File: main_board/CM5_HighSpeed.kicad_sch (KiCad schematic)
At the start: 16 parts, among them J1 USB3_A, J10 Conn_01x22_Female, J11 501568-0607-TR325, J12 SM04B-XSRS-ETBLFSN, J13 SM10B-XSRS-ETB, J22 690-019-298-412, U12 RT9742SNGV, U6 AP22653W6

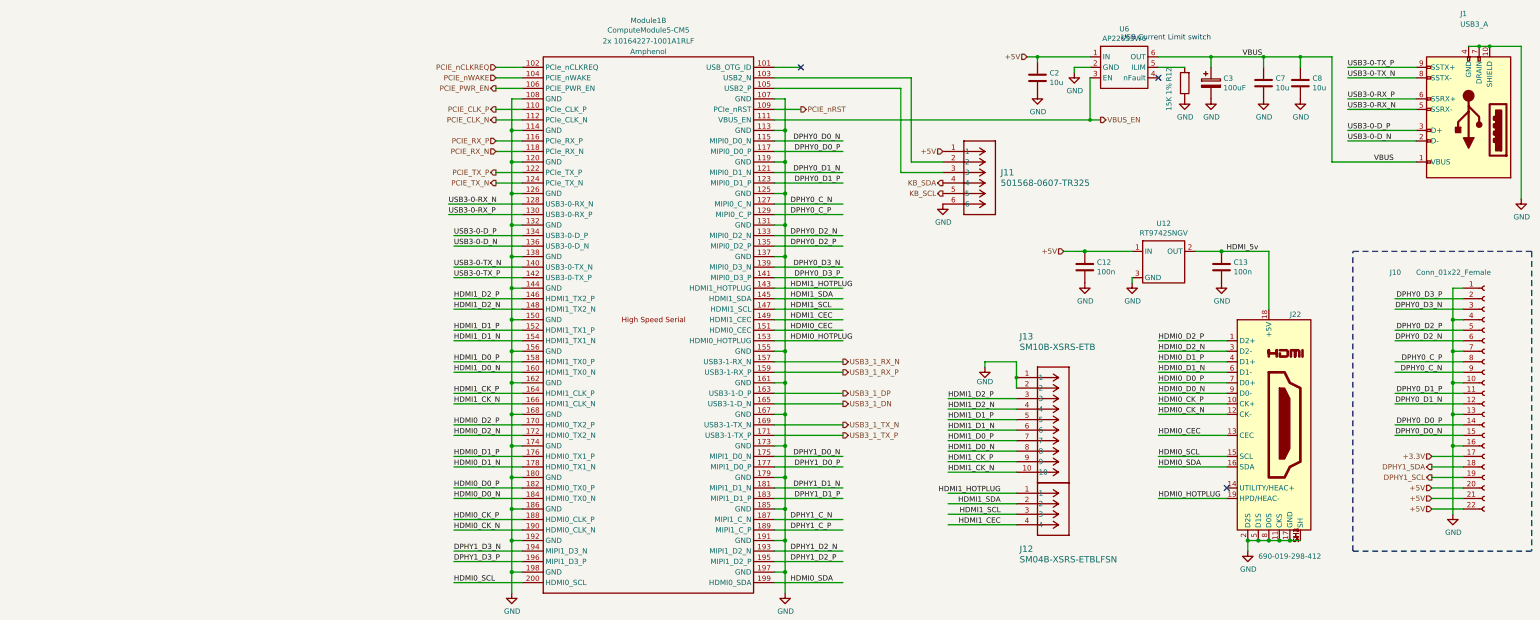
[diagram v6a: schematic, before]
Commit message: Add mounting points to symbols
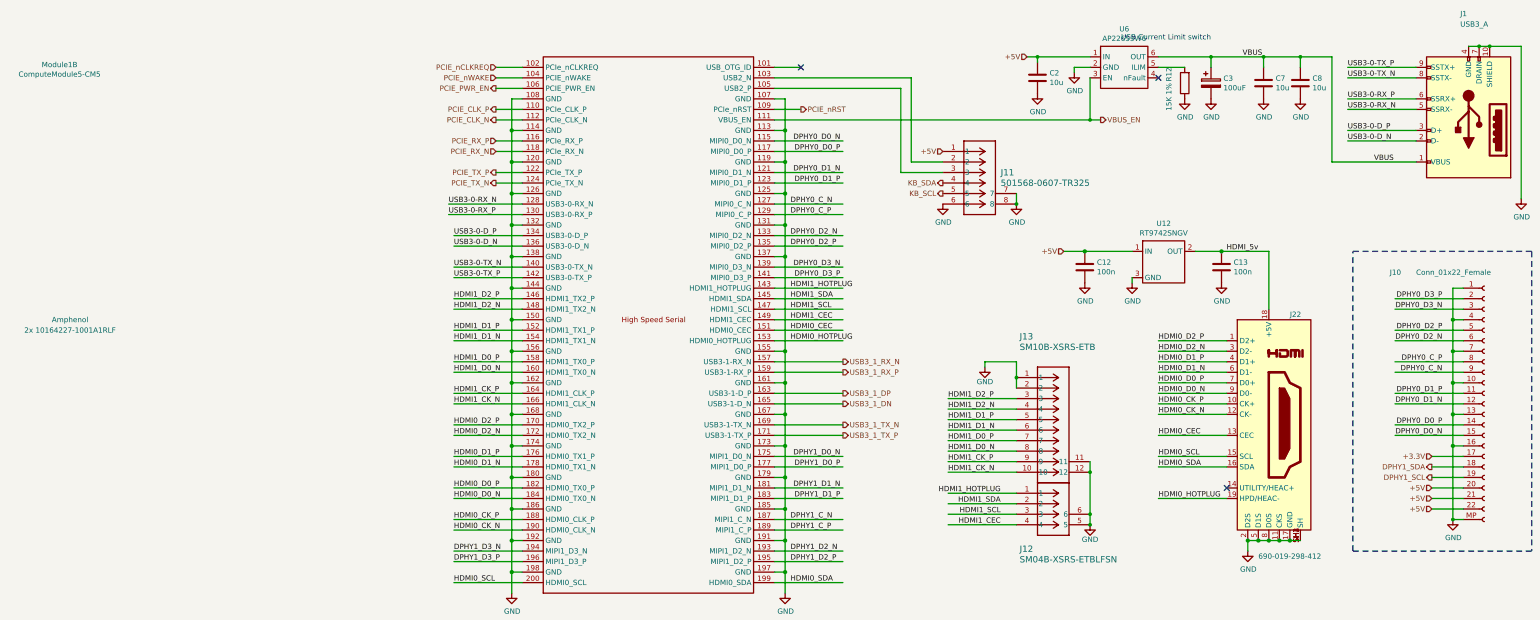
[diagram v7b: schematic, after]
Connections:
- net GND: now also J10.MP, J11.7, J11.8, J12.5, J12.6, J13.11, J13.12
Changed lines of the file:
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@@
 	)
 	(junction
+		(at 262.89 134.62)
+		(diameter 0)
+		(color 0 0 0 0)
+	)
+	(junction
 		(at 35.56 147.32)
 		(diameter 1.016)
@@
 	)
 	(junction
+		(at 157.48 58.42)
+		(diameter 0)
+		(color 0 0 0 0)
+	)
+	(junction
+		(at 175.26 135.89)
+		(diameter 0)
+		(color 0 0 0 0)
+	)
+	(junction
 		(at 35.56 78.74)
 		(diameter 1.016)
@@
 	)
 	(junction
+		(at 175.26 123.19)
+		(diameter 0)
+		(color 0 0 0 0)
+	)
+	(junction
 		(at 35.56 48.26)
 		(diameter 1.016)
@@
 	)
 	(junction
+		(at 175.26 133.35)
+		(diameter 0)
+		(color 0 0 0 0)
+	)
+	(junction
 		(at 35.56 124.46)
 		(diameter 1.016)
@@
 	(wire
 		(pts
+			(xy 157.48 55.88) (xy 157.48 58.42)
+		)
+		(stroke
+			(width 0)
+			(type default)
+		)
+	)
+	(wire
+		(pts
 			(xy 35.56 139.7) (xy 35.56 147.32)
 		)
@@
 	(wire
 		(pts
+			(xy 175.26 133.35) (xy 175.26 135.89)
+		)
+		(stroke
+			(width 0)
+			(type default)
+		)
+	)
+	(wire
+		(pts
 			(xy 171.45 25.4) (xy 171.45 26.67)
 		)
@@
 	(wire
 		(pts
+			(xy 262.89 134.62) (xy 265.43 134.62)
+		)
+		(stroke
+			(width 0)
+			(type default)
+		)
+	)
+	(wire
+		(pts
 			(xy 99.06 121.92) (xy 115.57 121.92)
 		)
@@
 	(wire
 		(pts
+			(xy 175.26 120.65) (xy 175.26 123.19)
+		)
+		(stroke
+			(width 0)
+			(type default)
+		)
+	)
+	(wire
+		(pts
 			(xy 20.32 60.96) (xy 38.1 60.96)
 		)
@@
 	(wire
 		(pts
+			(xy 175.26 123.19) (xy 175.26 133.35)
+		)
+		(stroke
+			(width 0)
+			(type default)
+		)
+	)
+	(wire
+		(pts
 			(xy 237.49 40.64) (xy 254 40.64)
 		)
@@
 	(wire
 		(pts
-			(xy 262.89 116.84) (xy 262.89 133.35)
+			(xy 262.89 116.84) (xy 262.89 134.62)
 		)
 		(stroke
@@
 		(dnp no)
 		(property "Reference" "Module1"
-			(at 68.58 14.097 0)
+			(at -73.66 24.765 0)
 			(effects
 				(font
@@
 		)
 		(property "Value" "ComputeModule5-CM5"
-			(at 68.58 16.4084 0)
+			(at -73.66 27.0764 0)
 			(effects
 				(font
@@
 		)
 		(property "Field4" "Amphenol"
-			(at 68.58 21.59 0)
+			(at -71.12 86.36 0)
 			(effects
 				(font
@@
 		)
 		(property "Field5" "2x 10164227-1001A1RLF"
-			(at 68.58 19.05 0)
+			(at -71.12 88.9 0)
 			(effects
 				(font
@@
 		(pin "200"
 		)
+		(pin "MP"
+		)
 		(instances
-			(project "CM5IO"
+			(project ""
+				(path "/e63e39d7-6ac0-4ffd-8aa3-1841a4541b55/00000000-0000-0000-0000-00005cff706a"
+					(reference "Module1")
+					(unit 2)
+				)
 				(path "/e63e39d7-6ac0-4ffd-8aa3-1841a4541b55/00000000-0000-0000-0000-00005cff70b1"
 					(reference "Module1")
@@
 		(pin "2"
 		)
+		(pin "7"
+		)
+		(pin "8"
+		)
 		(instances
 			(project ""
@@
 	)
 	(symbol
+		(lib_id "power:GND")
+		(at 175.26 135.89 0)
+		(unit 1)
+		(exclude_from_sim no)
+		(in_bom yes)
+		(on_board yes)
+		(dnp no)
+		(property "Reference" "#PWR057"
+			(at 175.26 142.24 0)
+			(effects
+				(font
+					(size 1.27 1.27)
+				)
+				(hide yes)
+			)
+		)
+		(property "Value" "GND"
+			(at 175.26 139.446 0)
+			(effects
+				(font
+					(size 1.27 1.27)
+				)
+			)
+		)
+		(property "Footprint" ""
+			(at 175.26 135.89 0)
+			(effects
+				(font
+					(size 1.27 1.27)
+				)
+				(hide yes)
+			)
+		)
+		(property "Datasheet" ""
+			(at 175.26 135.89 0)
+			(effects
+				(font
+					(size 1.27 1.27)
+				)
+				(hide yes)
+			)
+		)
+		(property "Description" "Power symbol creates a global label with name \"GND\" , ground"
+			(at 175.26 135.89 0)
+			(effects
+				(font
+					(size 1.27 1.27)
+				)
+				(hide yes)
+			)
+		)
+		(pin "1"
+		)
+		(instances
+			(project "main_board"
+				(path "/e63e39d7-6ac0-4ffd-8aa3-1841a4541b55/00000000-0000-0000-0000-00005cff70b1"
+					(reference "#PWR057")
+					(unit 1)
+				)
+			)
+		)
+	)
+	(symbol
 		(lib_id "Device:C")
 		(at 217.17 29.21 0)
@@
 		(pin "1"
 		)
+		(pin "5"
+		)
+		(pin "6"
+		)
 		(instances
 			(project ""
@@
 	(symbol
 		(lib_id "power:GND")
-		(at 262.89 133.35 0)
+		(at 262.89 134.62 0)
 		(unit 1)
 		(exclude_from_sim no)
@@
 		(dnp no)
 		(property "Reference" "#PWR075"
-			(at 262.89 139.7 0)
+			(at 262.89 140.97 0)
 			(effects
 				(font
@@
 		)
 		(property "Value" "GND"
-			(at 263.017 137.7442 0)
+			(at 263.017 139.0142 0)
 			(effects
 				(font
@@
 		)
 		(property "Footprint" ""
-			(at 262.89 133.35 0)
+			(at 262.89 134.62 0)
 			(effects
 				(font
@@
 		)
 		(property "Datasheet" ""
-			(at 262.89 133.35 0)
+			(at 262.89 134.62 0)
 			(effects
 				(font
@@
 		)
 		(property "Description" "Power symbol creates a global label with name \"GND\" , ground"
-			(at 262.89 133.35 0)
+			(at 262.89 134.62 0)
 			(effects
 				(font
@@
 	(symbol
 		(lib_id "power:GND")
+		(at 157.48 58.42 0)
+		(unit 1)
+		(exclude_from_sim no)
+		(in_bom yes)
+		(on_board yes)
+		(dnp no)
+		(property "Reference" "#PWR096"
+			(at 157.48 64.77 0)
+			(effects
+				(font
+					(size 1.27 1.27)
+				)
+				(hide yes)
+			)
+		)
+		(property "Value" "GND"
+			(at 157.607 62.8142 0)
+			(effects
+				(font
+					(size 1.27 1.27)
+				)
+			)
+		)
+		(property "Footprint" ""
+			(at 157.48 58.42 0)
+			(effects
+				(font
+					(size 1.27 1.27)
+				)
+				(hide yes)
+			)
+		)
+		(property "Datasheet" ""
+			(at 157.48 58.42 0)
+			(effects
+				(font
+					(size 1.27 1.27)
+				)
+				(hide yes)
+			)
+		)
+		(property "Description" "Power symbol creates a global label with name \"GND\" , ground"
+			(at 157.48 58.42 0)
+			(effects
+				(font
+					(size 1.27 1.27)
+				)
+				(hide yes)
+			)
+		)
+		(pin "1"
+		)
+		(instances
+			(project "main_board"
+				(path "/e63e39d7-6ac0-4ffd-8aa3-1841a4541b55/00000000-0000-0000-0000-00005cff70b1"
+					(reference "#PWR096")
+					(unit 1)
+				)
+			)
+		)
+	)
+	(symbol
+		(lib_id "power:GND")
 		(at 149.86 97.79 0)
 		(unit 1)
@@
 		(pin "9"
 		)
+		(pin "MP"
+		)
 		(instances
 			(project "main_board"
@@
 		(pin "3"
 		)
+		(pin "11"
+		)
+		(pin "12"
+		)
 		(instances

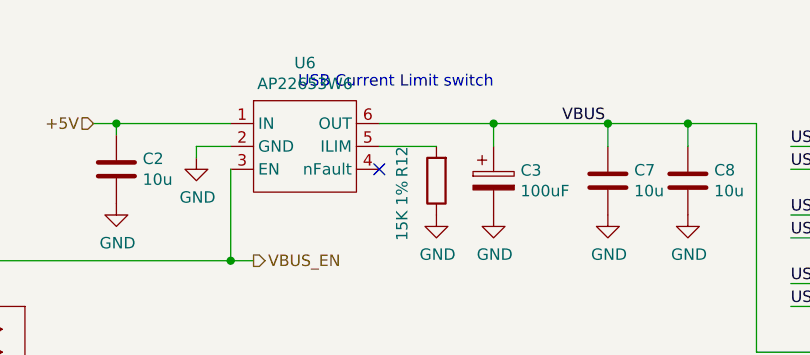
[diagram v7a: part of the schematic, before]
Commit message: Fix bad output voltage
For some reason I got 5V with previous values on prototype. Weird...
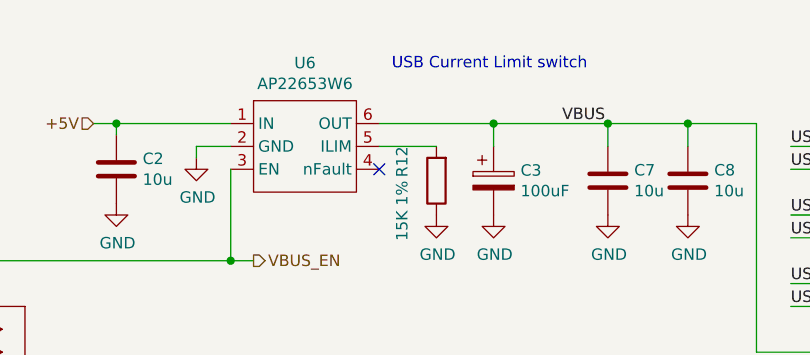
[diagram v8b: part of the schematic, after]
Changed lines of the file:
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@@
 	(text "USB Current Limit switch"
 		(exclude_from_sim no)
-		(at 204.47 19.05 0)
+		(at 214.884 17.018 0)
 		(effects
 			(font
